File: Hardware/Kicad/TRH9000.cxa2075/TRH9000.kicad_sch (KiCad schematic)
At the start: 5 parts, among them U1 74HC138, U2 74HC32

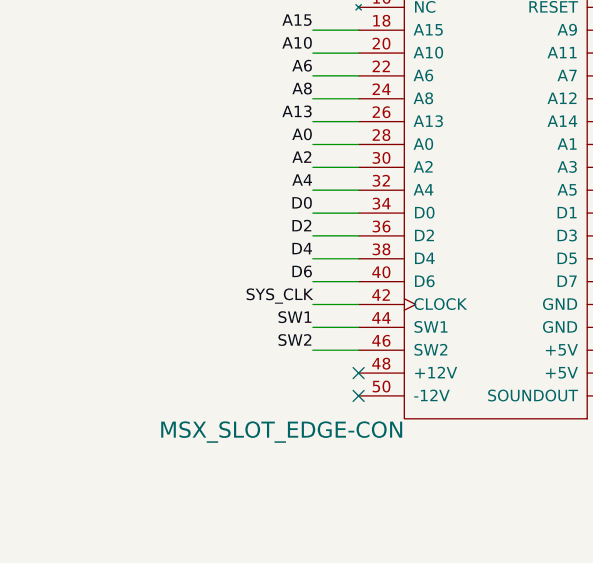
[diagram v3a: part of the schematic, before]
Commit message: SW1-SW2 jumper. v1.41
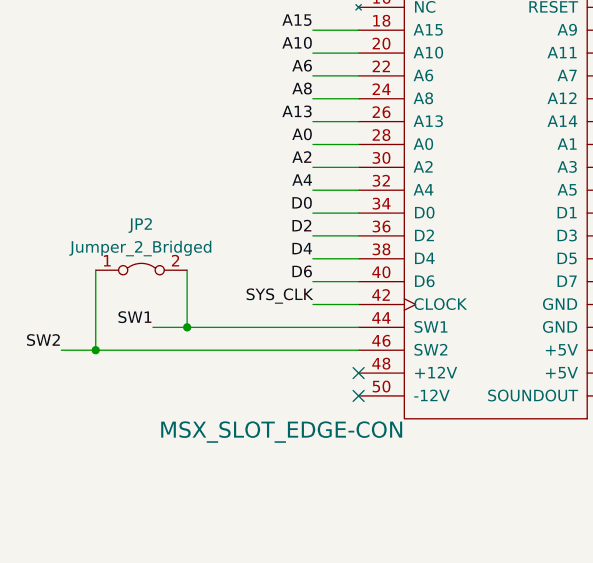
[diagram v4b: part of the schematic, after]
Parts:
- added JP2: Jumper_2_Bridged, Jumper:SolderJumper-2_P1.3mm_Bridged_Pad1.0x1.5mm, symbol Jumper:Jumper_2_Bridged
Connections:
- net SW1: now also JP2.2 (B)
- net SW2: now also JP2.1 (A)
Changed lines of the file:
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@@
   (title_block
     (title "TRH9000")
-    (date "2023-11-05")
-    (rev "1.4")
+    (date "2023-12-31")
+    (rev "1.41")
     (company "The Retro Hacker")
     (comment 2 "Shared under CERN-OHL-S license")
@@
   (junction (at 132.08 165.1) (diameter 0) (color 0 0 0 0)
   )
+  (junction (at 53.34 165.1) (diameter 0) (color 0 0 0 0)
+  )
   (junction (at 212.852 144.78) (diameter 0) (color 0 0 0 0)
+  )
+  (junction (at 63.5 162.56) (diameter 0) (color 0 0 0 0)
   )
   (junction (at 217.17 157.48) (diameter 0) (color 0 0 0 0)
@@
     (stroke (width 0) (type default))
   )
-  (wire (pts (xy 77.47 162.56) (xy 82.55 162.56))
+  (wire (pts (xy 59.69 162.56) (xy 63.5 162.56))
     (stroke (width 0) (type default))
   )
@@
     (stroke (width 0) (type default))
   )
-  (wire (pts (xy 77.47 165.1) (xy 82.55 165.1))
+  (wire (pts (xy 49.53 165.1) (xy 53.34 165.1))
     (stroke (width 0) (type default))
   )
@@
     (stroke (width 0) (type default))
   )
+  (wire (pts (xy 63.5 156.21) (xy 63.5 162.56))
+    (stroke (width 0) (type default))
+  )
   (wire (pts (xy 113.03 149.86) (xy 118.11 149.86))
     (stroke (width 0) (type default))
@@
     (stroke (width 0) (type default))
   )
+  (wire (pts (xy 53.34 156.21) (xy 53.34 165.1))
+    (stroke (width 0) (type default))
+  )
   (wire (pts (xy 113.03 127) (xy 118.11 127))
     (stroke (width 0) (type default))
@@
     (stroke (width 0) (type default))
   )
+  (wire (pts (xy 63.5 162.56) (xy 82.55 162.56))
+    (stroke (width 0) (type default))
+  )
   (wire (pts (xy 247.65 162.56) (xy 242.57 162.56))
     (stroke (width 0) (type default))
@@
   )
   (wire (pts (xy 139.7 160.02) (xy 139.7 162.56))
+    (stroke (width 0) (type default))
+  )
+  (wire (pts (xy 53.34 165.1) (xy 82.55 165.1))
     (stroke (width 0) (type default))
   )
@@
     (effects (font (size 1.27 1.27)) (justify right bottom))
   )
-  (label "SW1" (at 77.47 162.56 180) (fields_autoplaced)
+  (label "SW1" (at 59.69 162.56 180) (fields_autoplaced)
     (effects (font (size 1.27 1.27)) (justify right bottom))
   )
@@
     (effects (font (size 1.27 1.27)) (justify right bottom))
   )
-  (label "SW2" (at 77.47 165.1 180) (fields_autoplaced)
+  (label "SW2" (at 49.53 165.1 180) (fields_autoplaced)
     (effects (font (size 1.27 1.27)) (justify right bottom))
   )
@@
         )
       )
+    )
+  )
+  (symbol (lib_id "Jumper:Jumper_2_Bridged") (at 58.42 156.21 0) (unit 1)
+    (in_bom yes) (on_board yes) (dnp no) (fields_autoplaced)
+    (property "Reference" "JP2" (at 58.42 151.13 0)
+      (effects (font (size 1.27 1.27)))
+    )
+    (property "Value" "Jumper_2_Bridged" (at 58.42 153.67 0)
+      (effects (font (size 1.27 1.27)))
+    )
+    (property "Footprint" "Jumper:SolderJumper-2_P1.3mm_Bridged_Pad1.0x1.5mm" (at 58.42 156.21 0)
+      (effects (font (size 1.27 1.27)) hide)
+    )
+    (property "Datasheet" "~" (at 58.42 156.21 0)
+      (effects (font (size 1.27 1.27)) hide)
+    )
+    (pin "1")
+    (pin "2")
+    (instances
+      (project "TRH9000"
+        (path "/1a0ec755-0979-4213-9180-0cd879831c1c"
+          (reference "JP2") (unit 1)
+        )
+      )

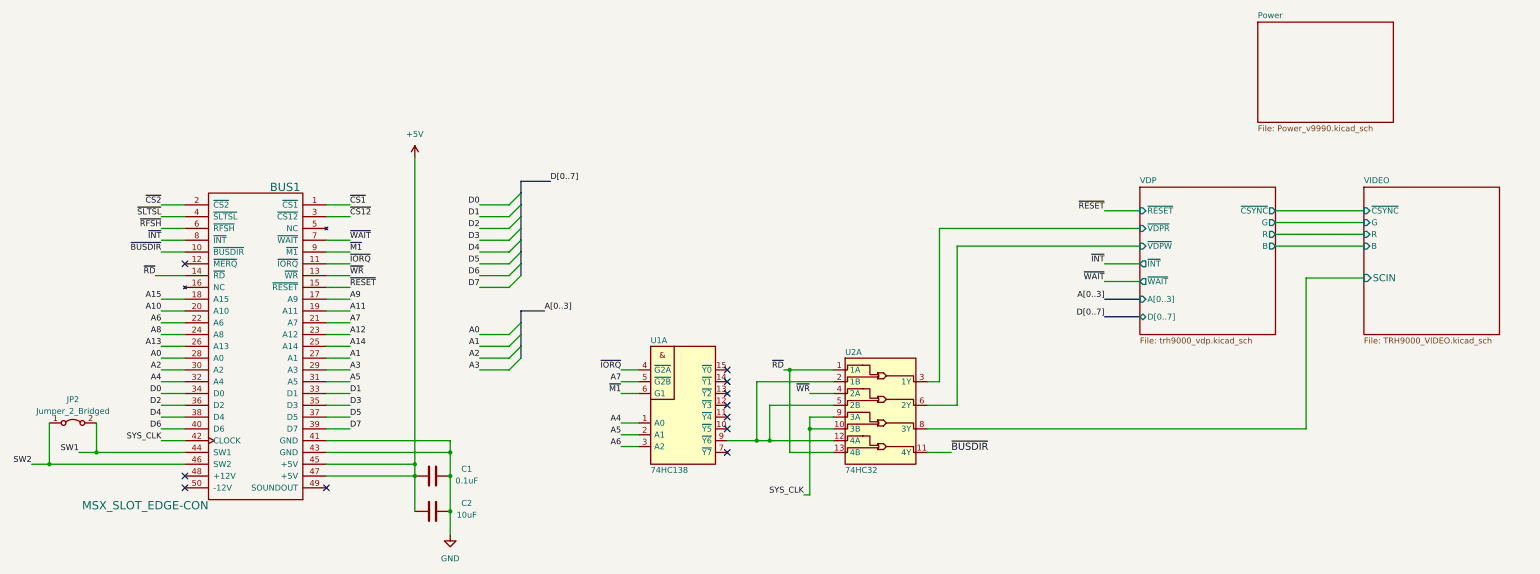
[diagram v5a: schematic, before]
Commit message: kicad 8 migration. minor positioning for the connectors
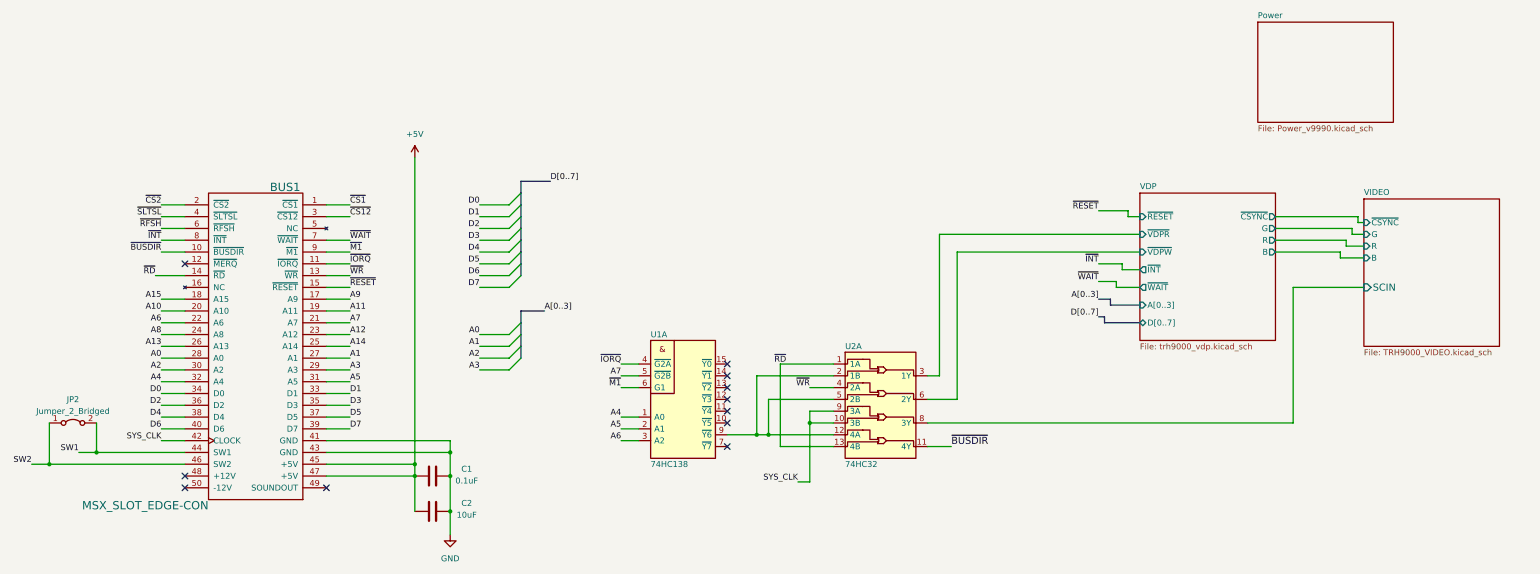
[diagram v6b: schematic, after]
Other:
- moved on the sheet: U1A, U2A
